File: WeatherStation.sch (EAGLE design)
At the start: 33 parts, among them J1 EDISON_CONNECTOR_FULLMOUNTING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, J2 EDISON_CONNECTOR_FULLHEADER, U1 MCP73831, U2 HTU21DSMD, U3 MPL3115A2LGA8, U4 PCA9306

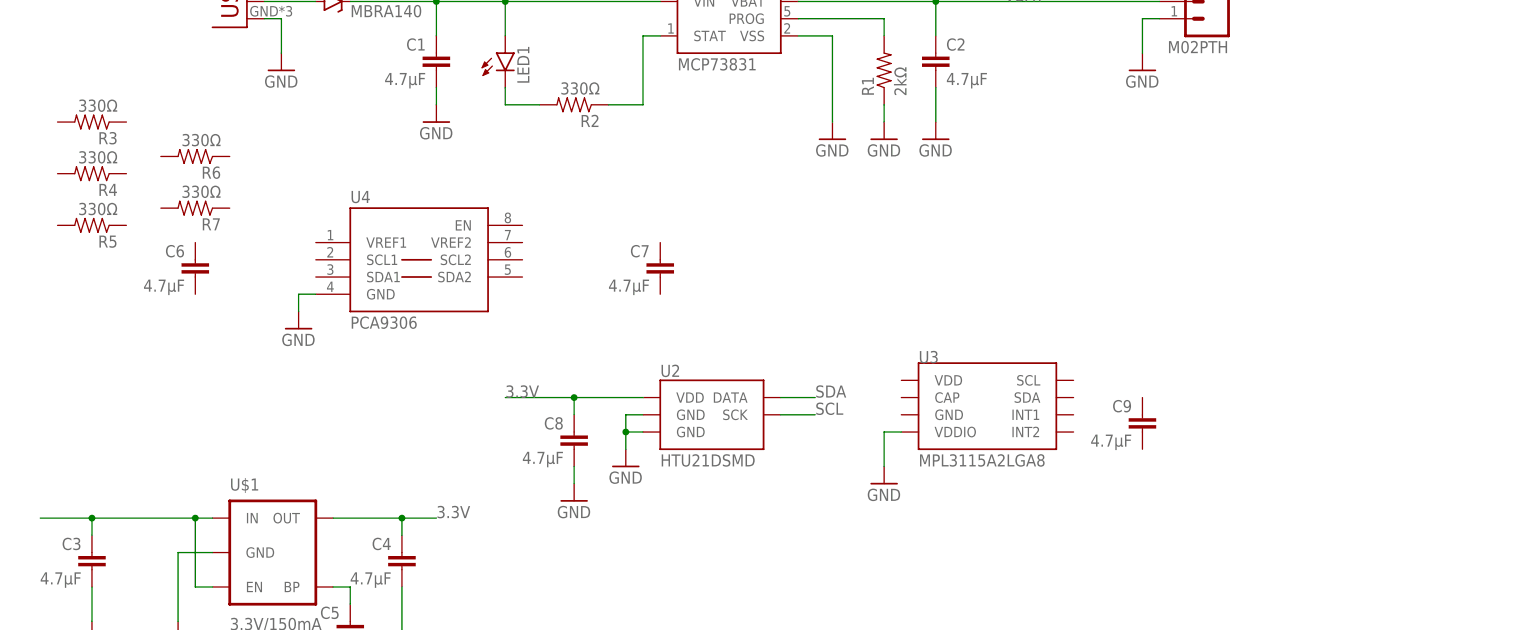
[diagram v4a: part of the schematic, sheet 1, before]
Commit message: connected schematic for MPL3115A2 and traces for HTU21D
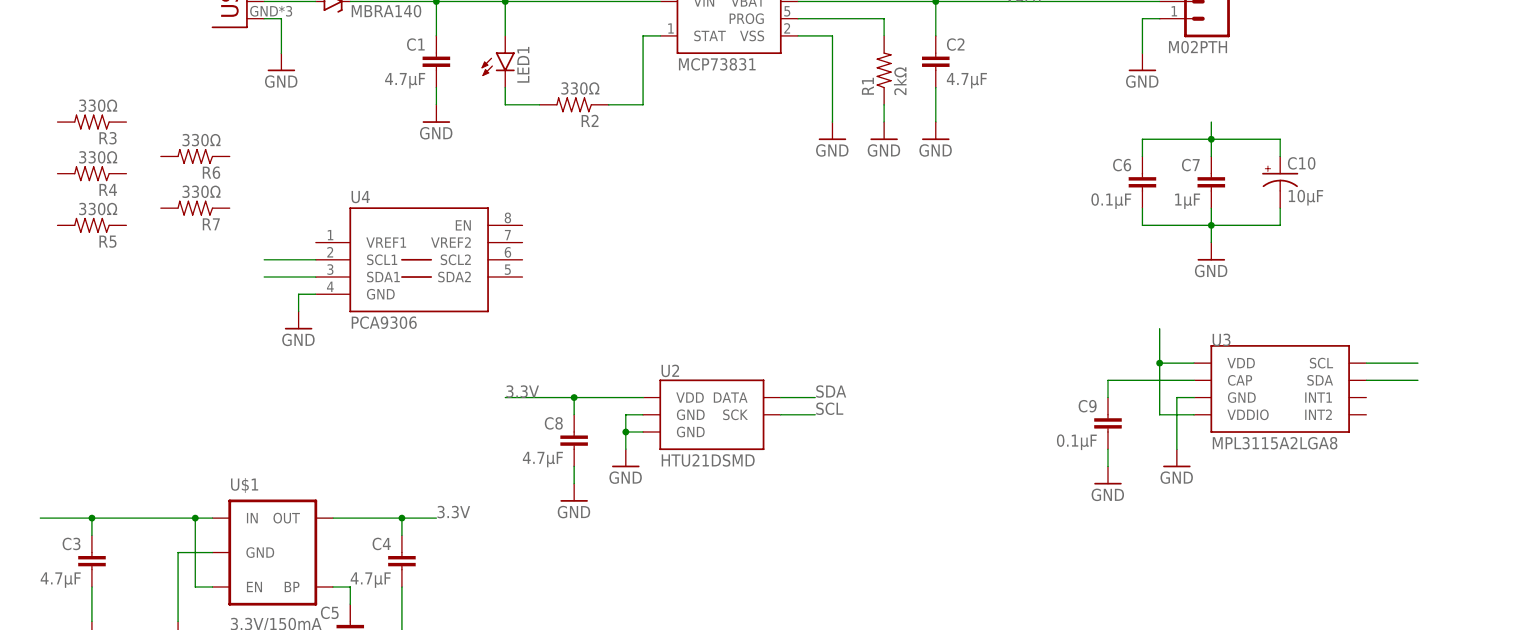
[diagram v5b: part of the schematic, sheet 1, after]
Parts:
- added C10: 10µF, SparkFun-Capacitors:CAP_POL1206
- C6, C9: value 4.7µF -> 0.1µF
- C7: value 4.7µF -> 1µF
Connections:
- new net N$10: U3.SDA
- new net N$3: C9.1, U3.CAP
- new net N$9: U3.SCL
- net 3.3V: now also C10.+, C6.1, C7.1, U3.VDD, U3.VDDIO
- net GND: now also C10.-, C6.2, C7.2, C9.2, U3.GND; no longer U3.VDDIO
- net SCL: now also U4.SCL1
- net SDA: now also U4.SDA1
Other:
- moved on the sheet: C6, C7, C9, U3
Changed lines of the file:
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@@
 <part name="GND13" library="SparkFun-Aesthetics" deviceset="GND" device=""/>
 <part name="GND14" library="SparkFun-Aesthetics" deviceset="GND" device=""/>
-<part name="C6" library="SparkFun-Capacitors" deviceset="CAP" device="0805" value="4.7µF"/>
-<part name="C7" library="SparkFun-Capacitors" deviceset="CAP" device="0805" value="4.7µF"/>
+<part name="C6" library="SparkFun-Capacitors" deviceset="CAP" device="0805" value="0.1µF"/>
+<part name="C7" library="SparkFun-Capacitors" deviceset="CAP" device="0805" value="1µF"/>
 <part name="R3" library="SparkFun-Resistors" deviceset="RESISTOR" device="0603-RES" value="330Ω"/>
 <part name="R4" library="SparkFun-Resistors" deviceset="RESISTOR" device="0603-RES" value="330Ω"/>
@@
 <part name="R7" library="SparkFun-Resistors" deviceset="RESISTOR" device="0603-RES" value="330Ω"/>
 <part name="C8" library="SparkFun-Capacitors" deviceset="CAP" device="0805" value="4.7µF"/>
-<part name="C9" library="SparkFun-Capacitors" deviceset="CAP" device="0805" value="4.7µF"/>
+<part name="C9" library="SparkFun-Capacitors" deviceset="CAP" device="0805" value="0.1µF"/>
 <part name="GND15" library="SparkFun-Aesthetics" deviceset="GND" device=""/>
+<part name="GND16" library="SparkFun-Aesthetics" deviceset="GND" device=""/>
+<part name="C10" library="SparkFun-Capacitors" deviceset="CAP_POL" device="1206" value="10µF"/>
+<part name="GND17" library="SparkFun-Aesthetics" deviceset="GND" device=""/>
 </parts>
 <sheets>
@@
 <instance part="GND8" gate="1" x="175.26" y="119.38"/>
 <instance part="U2" gate="U$1" x="111.76" y="68.58"/>
-<instance part="U3" gate="G$1" x="152.4" y="71.12"/>
+<instance part="U3" gate="G$1" x="195.58" y="73.66"/>
 <instance part="U4" gate="G$1" x="68.58" y="88.9"/>
 <instance part="U$1" gate="G$1" x="48.26" y="48.26"/>
-<instance part="GND9" gate="1" x="137.16" y="58.42"/>
+<instance part="GND9" gate="1" x="180.34" y="60.96"/>
 <instance part="GND10" gate="1" x="99.06" y="60.96"/>
 <instance part="GND11" gate="1" x="50.8" y="81.28"/>
@@
 <instance part="GND13" gate="1" x="20.32" y="35.56"/>
 <instance part="GND14" gate="1" x="58.42" y="25.4"/>
-<instance part="C6" gate="G$1" x="35.56" y="88.9" rot="MR0"/>
-<instance part="C7" gate="G$1" x="104.14" y="88.9" rot="MR0"/>
+<instance part="C6" gate="G$1" x="175.26" y="101.6" rot="MR0"/>
+<instance part="C7" gate="G$1" x="185.42" y="101.6" rot="MR0"/>
 <instance part="R3" gate="G$1" x="20.32" y="111.76" rot="R180"/>
 <instance part="R4" gate="G$1" x="20.32" y="104.14" rot="R180"/>
@@
 <instance part="R7" gate="G$1" x="35.56" y="99.06" rot="R180"/>
 <instance part="C8" gate="G$1" x="91.44" y="63.5" rot="MR0"/>
-<instance part="C9" gate="G$1" x="175.26" y="66.04" rot="MR0"/>
+<instance part="C9" gate="G$1" x="170.18" y="66.04" rot="MR0"/>
 <instance part="GND15" gate="1" x="91.44" y="55.88"/>
+<instance part="GND16" gate="1" x="170.18" y="58.42"/>
+<instance part="C10" gate="G$1" x="195.58" y="104.14"/>
+<instance part="GND17" gate="1" x="185.42" y="91.44"/>
 </instances>
 <busses>
@@
 <segment>
 <pinref part="GND9" gate="1" pin="GND"/>
-<pinref part="U3" gate="G$1" pin="VDDIO"/>
-<wire x1="137.16" y1="60.96" x2="137.16" y2="66.04" width="0.1524" layer="91"/>
-<wire x1="137.16" y1="66.04" x2="139.7" y2="66.04" width="0.1524" layer="91"/>
+<wire x1="180.34" y1="63.5" x2="180.34" y2="71.12" width="0.1524" layer="91"/>
+<pinref part="U3" gate="G$1" pin="GND"/>
+<wire x1="182.88" y1="71.12" x2="180.34" y2="71.12" width="0.1524" layer="91"/>
 </segment>
 <segment>
@@
 <wire x1="91.44" y1="60.96" x2="91.44" y2="58.42" width="0.1524" layer="91"/>
 </segment>
+<segment>
+<pinref part="C9" gate="G$1" pin="2"/>
+<pinref part="GND16" gate="1" pin="GND"/>
+<wire x1="170.18" y1="63.5" x2="170.18" y2="60.96" width="0.1524" layer="91"/>
+</segment>
+<segment>
+<pinref part="C6" gate="G$1" pin="2"/>
+<wire x1="175.26" y1="99.06" x2="175.26" y2="96.52" width="0.1524" layer="91"/>
+<wire x1="175.26" y1="96.52" x2="185.42" y2="96.52" width="0.1524" layer="91"/>
+<pinref part="C10" gate="G$1" pin="-"/>
+<wire x1="185.42" y1="96.52" x2="195.58" y2="96.52" width="0.1524" layer="91"/>
+<wire x1="195.58" y1="96.52" x2="195.58" y2="99.06" width="0.1524" layer="91"/>
+<pinref part="C7" gate="G$1" pin="2"/>
+<wire x1="185.42" y1="99.06" x2="185.42" y2="96.52" width="0.1524" layer="91"/>
+<junction x="185.42" y="96.52"/>
+<pinref part="GND17" gate="1" pin="GND"/>
+<wire x1="185.42" y1="96.52" x2="185.42" y2="93.98" width="0.1524" layer="91"/>
+</segment>
 </net>
 <net name="VBAT" class="0">
@@
 <junction x="91.44" y="71.12"/>
 <label x="81.28" y="71.12" size="1.778" layer="95"/>
+</segment>
+<segment>
+<pinref part="U3" gate="G$1" pin="VDDIO"/>
+<wire x1="182.88" y1="68.58" x2="177.8" y2="68.58" width="0.1524" layer="91"/>
+<wire x1="177.8" y1="68.58" x2="177.8" y2="76.2" width="0.1524" layer="91"/>
+<pinref part="U3" gate="G$1" pin="VDD"/>
+<wire x1="177.8" y1="76.2" x2="177.8" y2="81.28" width="0.1524" layer="91"/>
+<wire x1="182.88" y1="76.2" x2="177.8" y2="76.2" width="0.1524" layer="91"/>
+<junction x="177.8" y="76.2"/>
+</segment>
+<segment>
+<pinref part="C6" gate="G$1" pin="1"/>
+<wire x1="175.26" y1="109.22" x2="175.26" y2="106.68" width="0.1524" layer="91"/>
+<pinref part="C10" gate="G$1" pin="+"/>
+<wire x1="175.26" y1="109.22" x2="185.42" y2="109.22" width="0.1524" layer="91"/>
+<wire x1="185.42" y1="109.22" x2="195.58" y2="109.22" width="0.1524" layer="91"/>
+<wire x1="195.58" y1="109.22" x2="195.58" y2="106.68" width="0.1524" layer="91"/>
+<pinref part="C7" gate="G$1" pin="1"/>
+<wire x1="185.42" y1="106.68" x2="185.42" y2="109.22" width="0.1524" layer="91"/>
+<junction x="185.42" y="109.22"/>
+<wire x1="185.42" y1="111.76" x2="185.42" y2="109.22" width="0.1524" layer="91"/>
 </segment>
 </net>
@@
 <label x="127" y="71.12" size="1.778" layer="95"/>
 </segment>
+<segment>
+<pinref part="U4" gate="G$1" pin="SDA1"/>
+<wire x1="45.72" y1="88.9" x2="53.34" y2="88.9" width="0.1524" layer="91"/>
+</segment>
 </net>
 <net name="SCL" class="0">
@@
 <label x="127" y="68.58" size="1.778" layer="95"/>
 </segment>
-</net>
+<segment>
+<pinref part="U4" gate="G$1" pin="SCL1"/>
+<wire x1="45.72" y1="91.44" x2="53.34" y2="91.44" width="0.1524" layer="91"/>
+</segment>
+</net>
+<net name="N$3" class="0">
+<segment>
+<pinref part="U3" gate="G$1" pin="CAP"/>
+<pinref part="C9" gate="G$1" pin="1"/>
+<wire x1="182.88" y1="73.66" x2="170.18" y2="73.66" width="0.1524" layer="91"/>
+<wire x1="170.18" y1="73.66" x2="170.18" y2="71.12" width="0.1524" layer="91"/>
+</segment>
+</net>
+<net name="N$9" class="0">
+<segment>
+<pinref part="U3" gate="G$1" pin="SCL"/>
+<wire x1="215.9" y1="76.2" x2="208.28" y2="76.2" width="0.1524" layer="91"/>
+</segment>
+</net>
+<net name="N$10" class="0">
+<segment>
+<pinref part="U3" gate="G$1" pin="SDA"/>
+<wire x1="215.9" y1="73.66" x2="208.28" y2="73.66" width="0.1524" layer="91"/>
+</segment>
+</net>

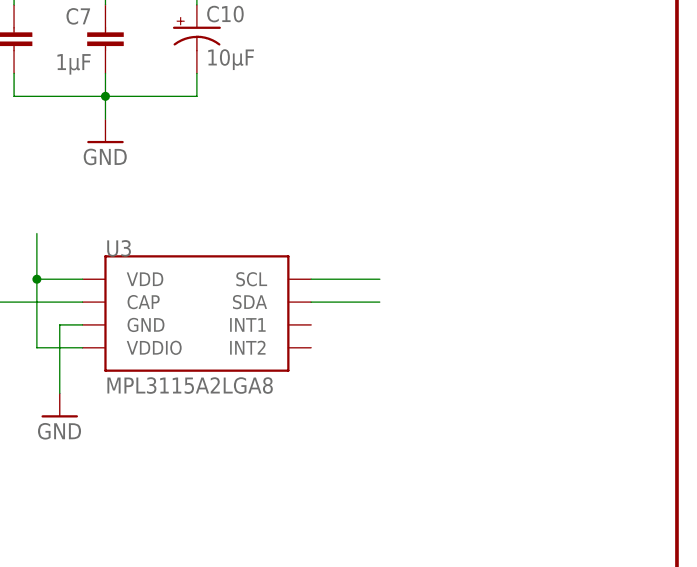
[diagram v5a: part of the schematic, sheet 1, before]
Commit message: set and drew traces for MPL3115A2
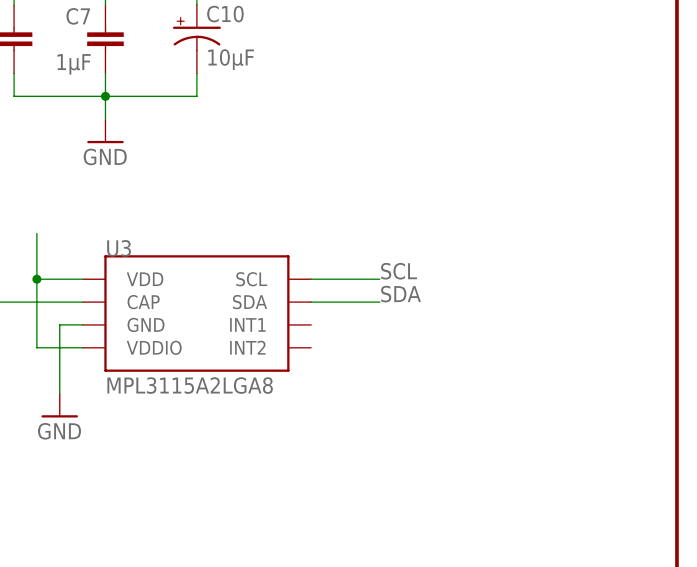
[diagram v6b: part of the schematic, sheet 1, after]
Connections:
- removed net N$10: U3.SDA
- removed net N$9: U3.SCL
- net SCL: now also U3.SCL
- net SDA: now also U3.SDA
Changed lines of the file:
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@@
 <wire x1="45.72" y1="88.9" x2="53.34" y2="88.9" width="0.1524" layer="91"/>
+</segment>
+<segment>
+<pinref part="U3" gate="G$1" pin="SDA"/>
+<wire x1="215.9" y1="73.66" x2="208.28" y2="73.66" width="0.1524" layer="91"/>
+<label x="215.9" y="73.66" size="1.778" layer="95"/>
 </segment>
 </net>
@@
 <wire x1="45.72" y1="91.44" x2="53.34" y2="91.44" width="0.1524" layer="91"/>
 </segment>
+<segment>
+<pinref part="U3" gate="G$1" pin="SCL"/>
+<wire x1="215.9" y1="76.2" x2="208.28" y2="76.2" width="0.1524" layer="91"/>
+<label x="215.9" y="76.2" size="1.778" layer="95"/>
+</segment>
 </net>
 <net name="N$3" class="0">
@@
 </segment>
 </net>
-<net name="N$9" class="0">
-<segment>
-<pinref part="U3" gate="G$1" pin="SCL"/>
-<wire x1="215.9" y1="76.2" x2="208.28" y2="76.2" width="0.1524" layer="91"/>
-</segment>
-</net>
-<net name="N$10" class="0">
-<segment>
-<pinref part="U3" gate="G$1" pin="SDA"/>
-<wire x1="215.9" y1="73.66" x2="208.28" y2="73.66" width="0.1524" layer="91"/>
-</segment>
-</net>

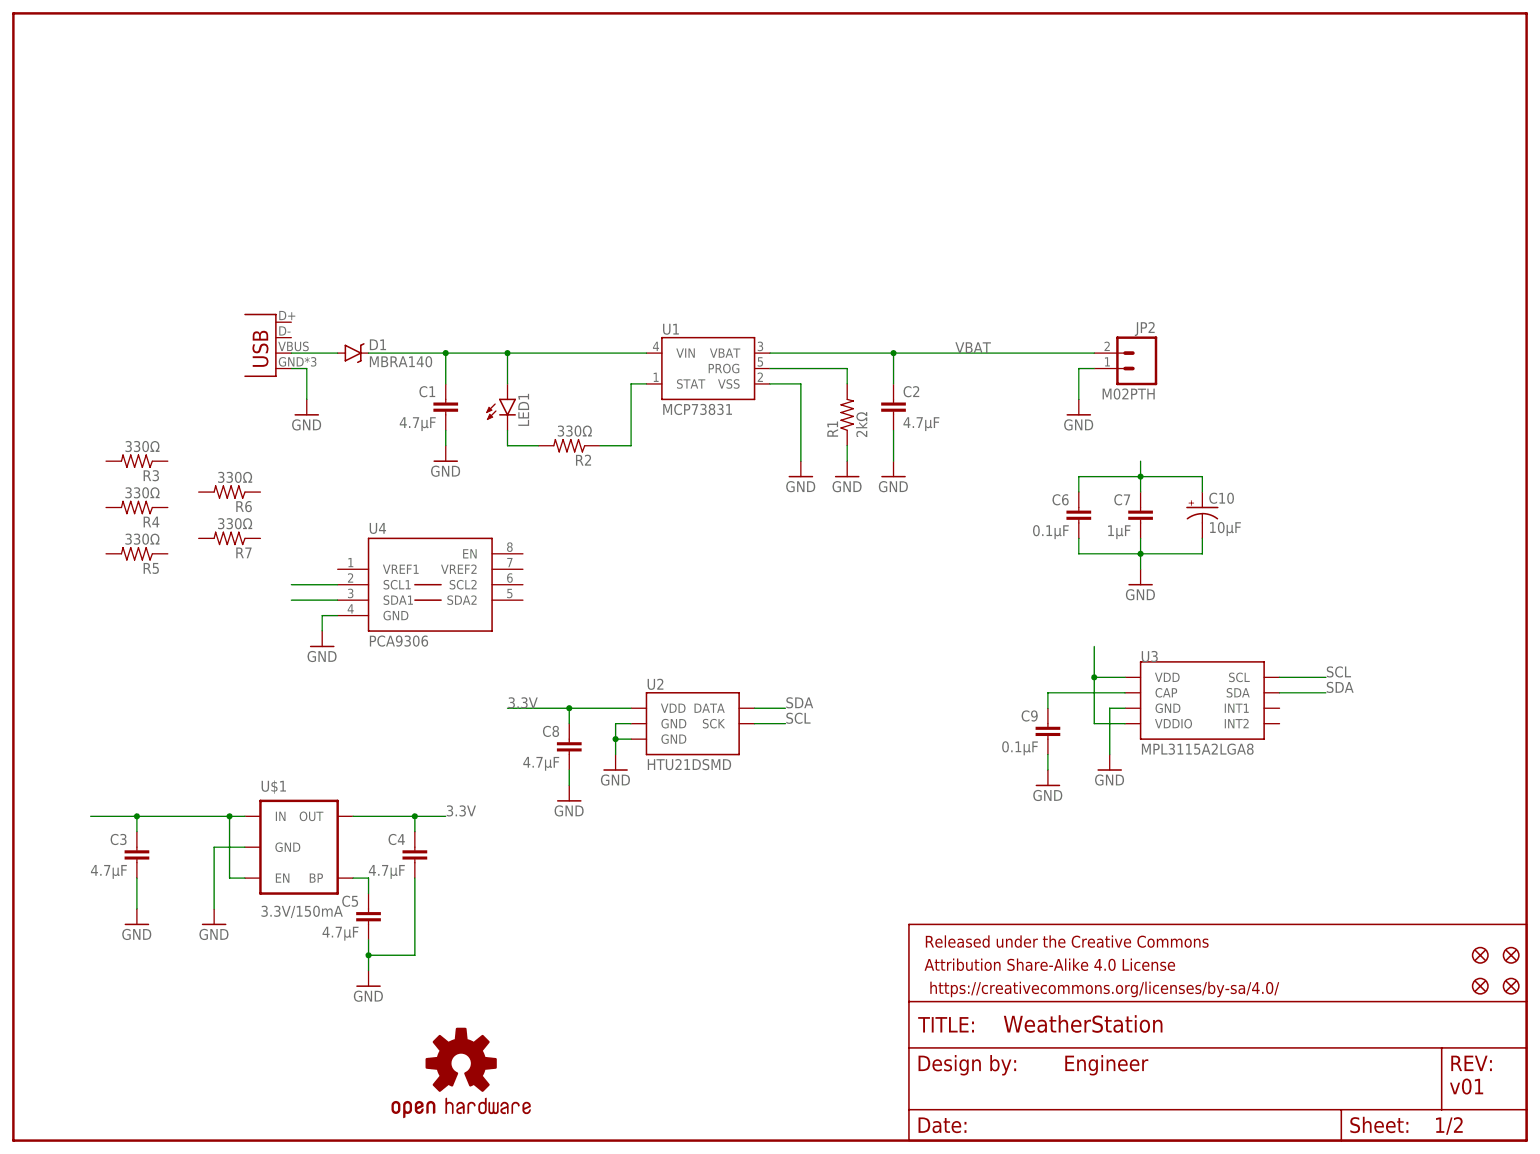
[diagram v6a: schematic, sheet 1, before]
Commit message: set and drew traces for MIC5205
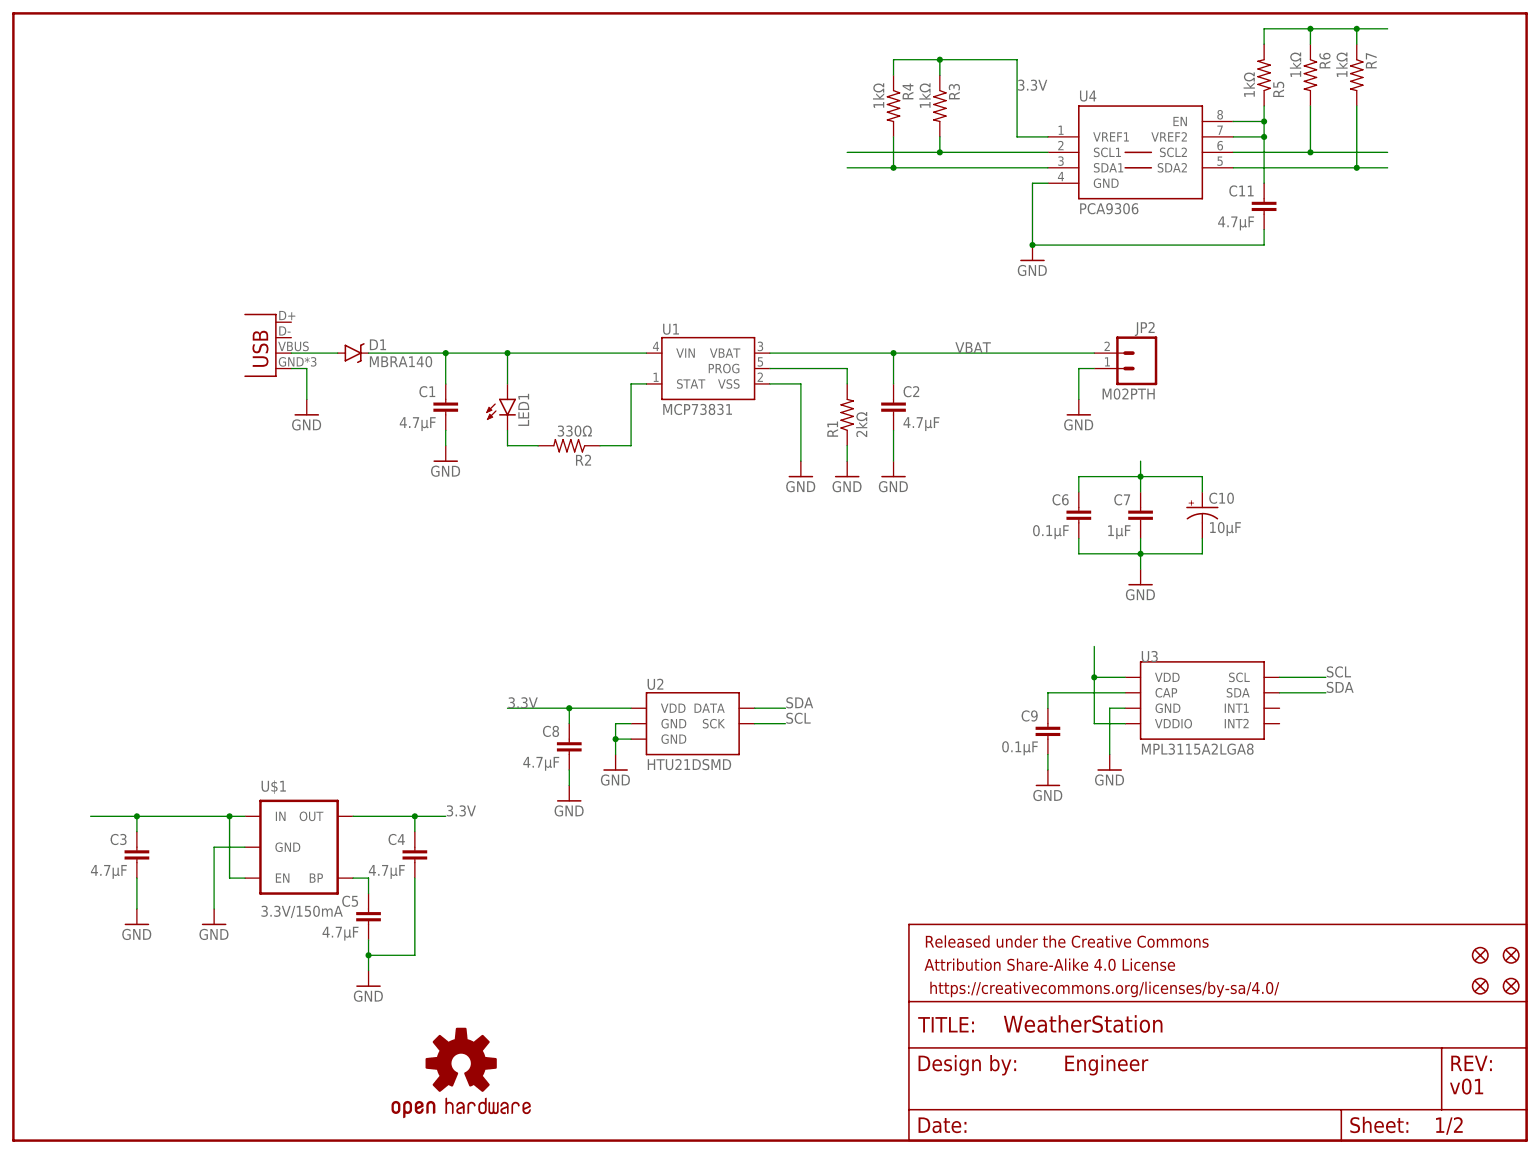
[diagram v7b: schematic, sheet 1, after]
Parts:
- added C11: 4.7µF, SparkFun-Capacitors:CAP0805
- R3, R4, R5, R6, R7: value 330Ω -> 1kΩ
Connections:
- removed net N$7: C3.1, U$1.EN, U$1.IN
- new net N$10: C11.1, R5.1, U4.EN, U4.VREF2
- new net N$11: R6.2, U4.SCL2
- new net N$12: R7.2, U4.SDA2
- net 1.8V: now also R5.2, R6.1, R7.1
- net 3.3V: now also R3.1, R4.1, U4.VREF1
- net GND: now also C11.2
- net SCL: now also R3.2
- net SDA: now also R4.2
- net VBAT: now also C3.1, U$1.EN, U$1.IN
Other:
- moved on the sheet: R3, R4, R5, R6, R7, U4
